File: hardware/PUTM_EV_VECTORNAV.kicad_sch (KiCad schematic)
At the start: 0 parts

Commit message: Fixes after review
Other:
- sheet MCU ports: added VN_GNSS_SYNC; removed VN_SNC_IN, VN_SNC_OUT
- sheet VectorNav ports: added GNSS_SYNC; removed SNC_IN, SNC_OUT
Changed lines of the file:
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@@
-	(wire
-		(pts
-			(xy 82.55 111.76) (xy 120.65 111.76)
-		)
-		(stroke
-			(width 0)
-			(type default)
-		)
-	)
 	(wire
 		(pts
@@
 			)
 		)
-		(pin "CAN_RX" input
+		(pin "CAN_RX" output
 			(at 204.47 87.63 180)
 			(effects
@@
 			)
 		)
-		(pin "CAN_RX" input
-			(at 171.45 85.09 0)
-			(effects
-				(font
-					(size 1.27 1.27)
-				)
-				(justify right)
-			)
-		)
-		(pin "CAN_TX" input
-			(at 171.45 87.63 0)
-			(effects
-				(font
-					(size 1.27 1.27)
-				)
-				(justify right)
-			)
-		)
 		(pin "VN_CS" input
 			(at 120.65 82.55 180)
@@
 			)
 		)
-		(pin "VN_RX" input
-			(at 120.65 97.79 180)
-			(effects
-				(font
-					(size 1.27 1.27)
-				)
-				(justify left)
-			)
-		)
 		(pin "VN_SCK" input
 			(at 120.65 90.17 180)
@@
 			)
 		)
-		(pin "VN_SNC_IN" input
-			(at 120.65 111.76 180)
-			(effects
-				(font
-					(size 1.27 1.27)
-				)
-				(justify left)
-			)
-		)
-		(pin "VN_SNC_OUT" output
-			(at 120.65 114.3 180)
-			(effects
-				(font
-					(size 1.27 1.27)
-				)
-				(justify left)
-			)
-		)
-		(pin "VN_TX" output
-			(at 120.65 95.25 180)
-			(effects
-				(font
-					(size 1.27 1.27)
-				)
-				(justify left)
-			)
-		)
-		(pin "CAN_STBY" input
+		(pin "CAN_STBY" output
 			(at 171.45 90.17 0)
 			(effects
@@
 				)
 				(justify right)
+			)
+		)
+		(pin "VN_RX" input
+			(at 120.65 95.25 180)
+			(effects
+				(font
+					(size 1.27 1.27)
+				)
+				(justify left)
+			)
+		)
+		(pin "VN_TX" output
+			(at 120.65 97.79 180)
+			(effects
+				(font
+					(size 1.27 1.27)
+				)
+				(justify left)
+			)
+		)
+		(pin "CAN_RX" input
+			(at 171.45 87.63 0)
+			(effects
+				(font
+					(size 1.27 1.27)
+				)
+				(justify right)
+			)
+		)
+		(pin "CAN_TX" output
+			(at 171.45 85.09 0)
+			(effects
+				(font
+					(size 1.27 1.27)
+				)
+				(justify right)
+			)
+		)
+		(pin "VN_GNSS_SYNC" input
+			(at 120.65 114.3 180)
+			(effects
+				(font
+					(size 1.27 1.27)
+				)
+				(justify left)
 			)
 		)
@@
 			)
 		)
-		(pin "SNC_IN" input
-			(at 82.55 111.76 0)
-			(effects
-				(font
-					(size 1.27 1.27)
-				)
-				(justify right)
-			)
-		)
-		(pin "SNC_OUT" output
-			(at 82.55 114.3 0)
-			(effects
-				(font
-					(size 1.27 1.27)
-				)
-				(justify right)
-			)
-		)
 		(pin "TX1" output
 			(at 64.77 76.2 90)
@@
 			(effects
 				(font
+					(size 1.27 1.27)
+				)
+				(justify right)
+			)
+		)
+		(pin "GNSS_SYNC" input
+			(at 82.55 114.3 0)
+			(effects
+				(font

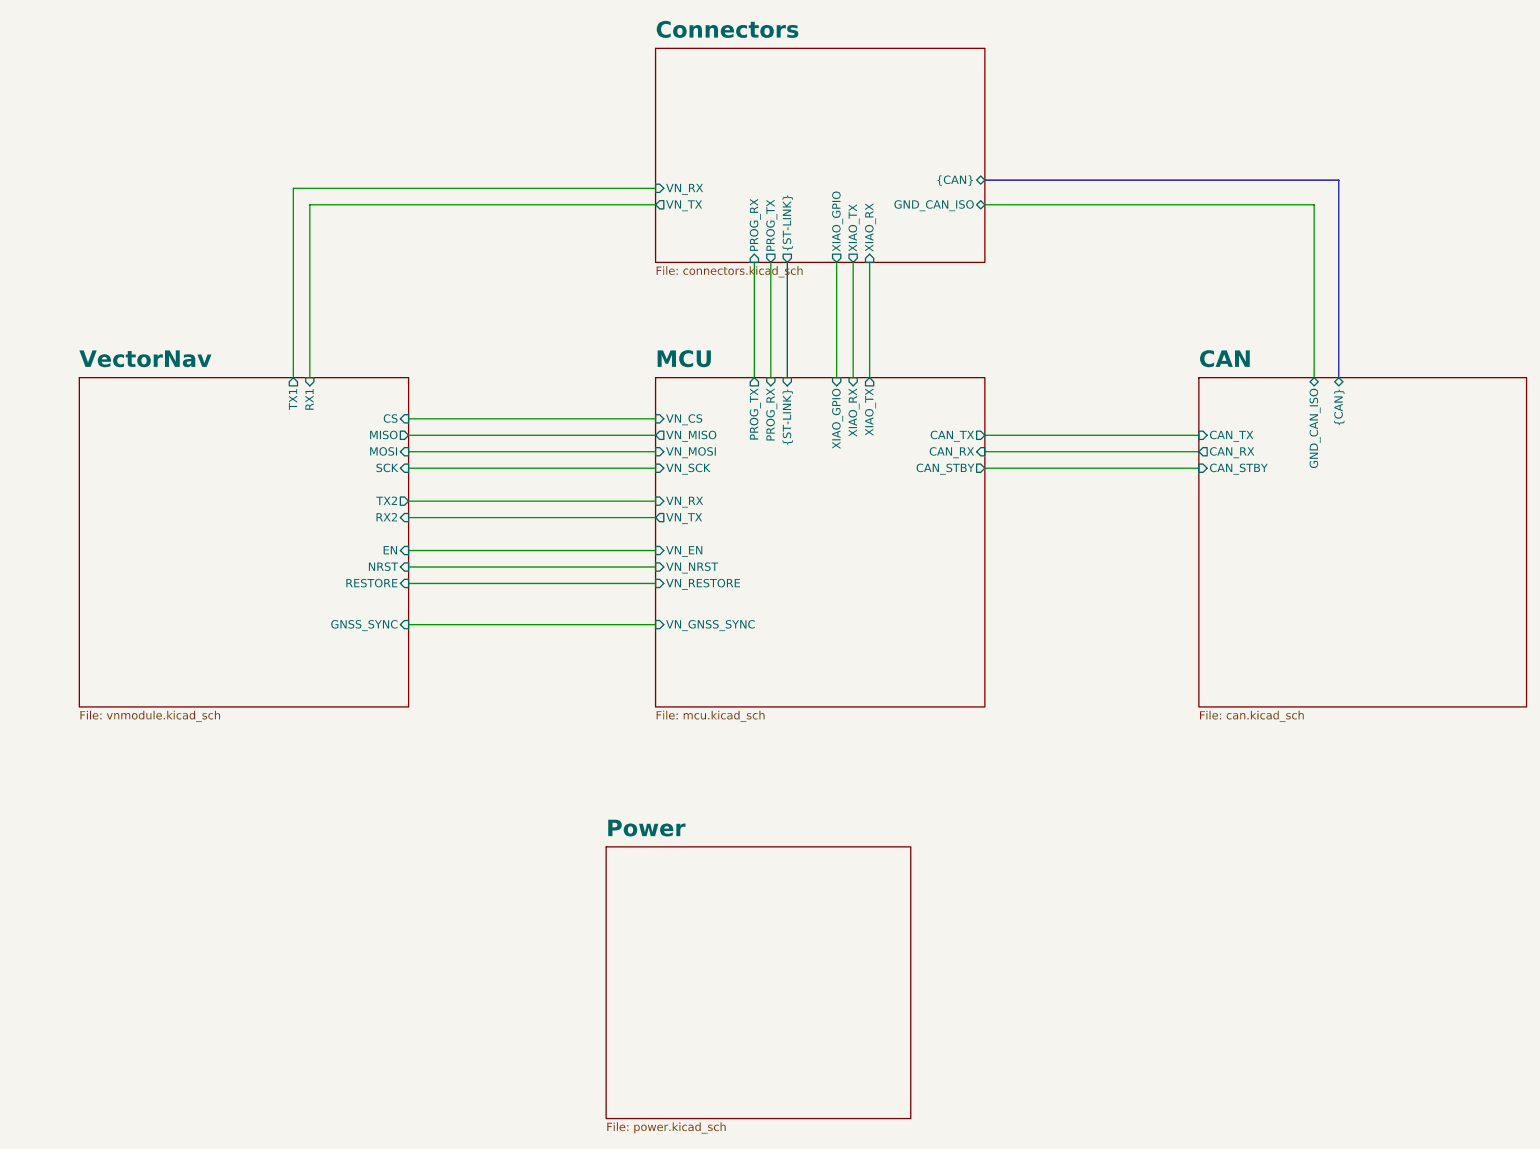
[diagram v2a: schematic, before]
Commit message: Fixes after review and mouser links for most components added
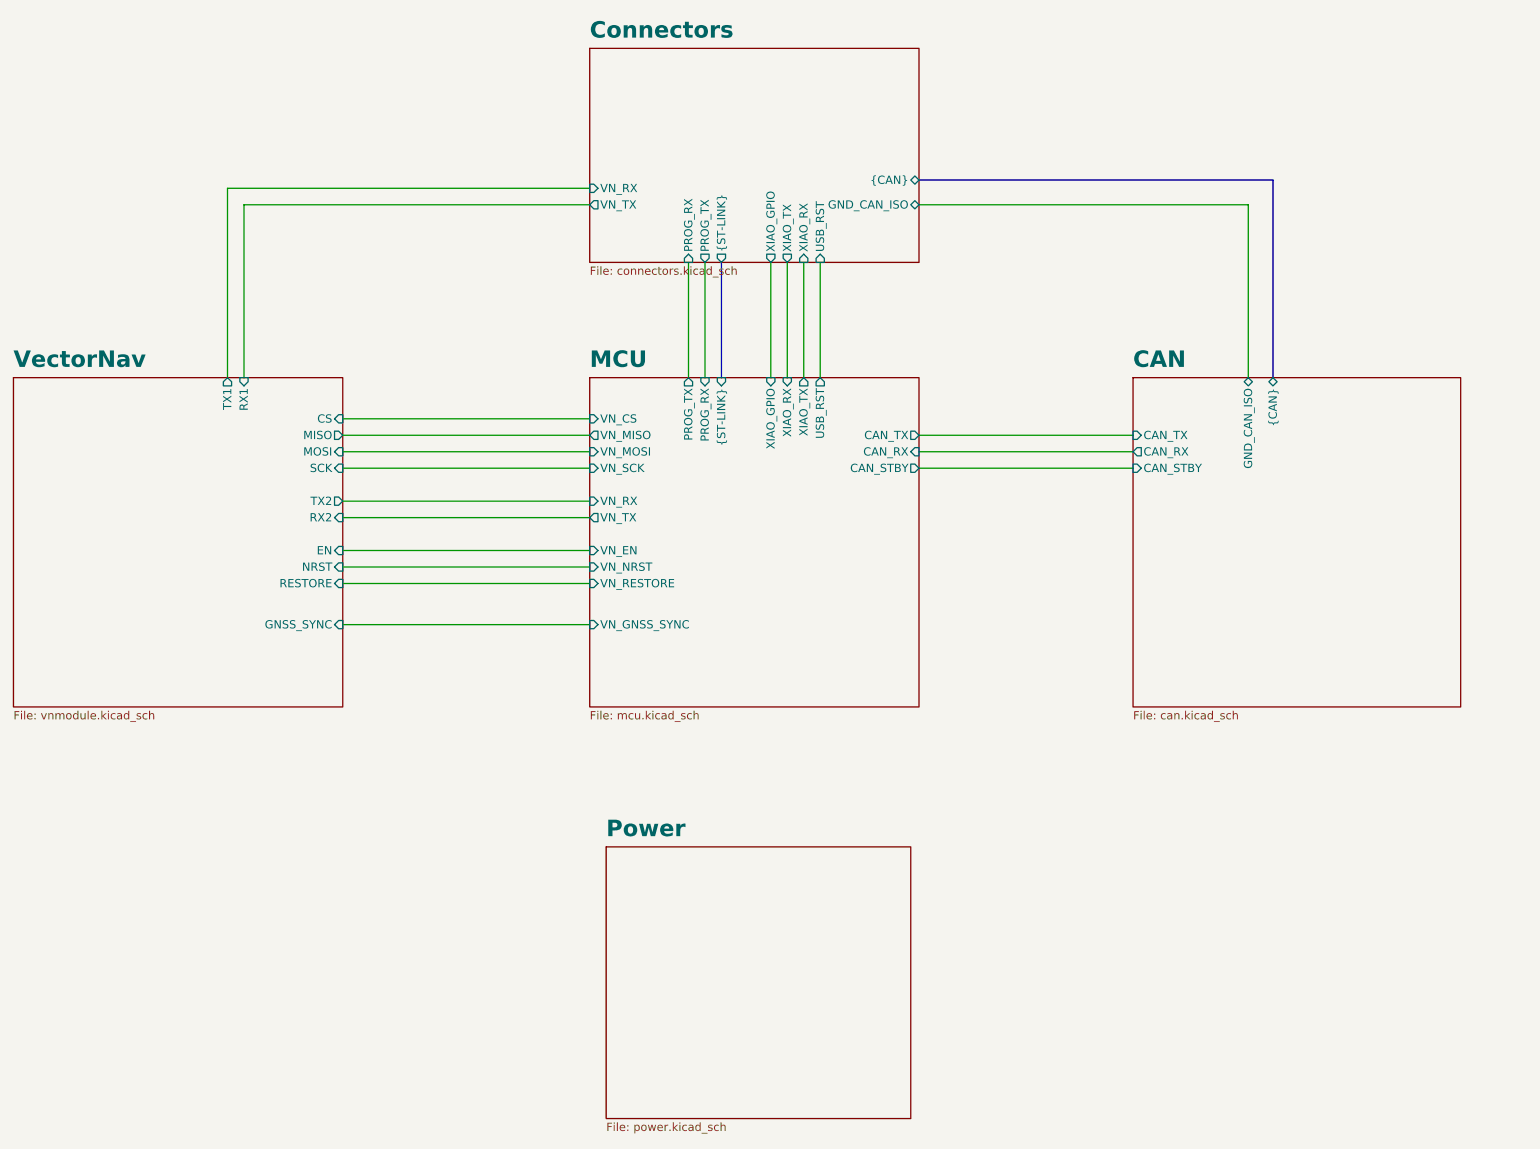
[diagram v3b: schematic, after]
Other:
- sheet Connectors ports: added USB_RST; removed none
- sheet MCU ports: added USB_RST; removed none

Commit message: Some smaller fixes and final aesthetic changes
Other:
- company: Author: -> Author: Kacper Pawlak
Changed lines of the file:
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@@
 	(title_block
 		(rev "${REVISION}")
-		(company "Author:")
-		(comment 1 "Reviewer:")
+		(company "Author: Kacper Pawlak")
+		(comment 1 "Reviewer: Piotr Lesicki")
 	)
 	(wire

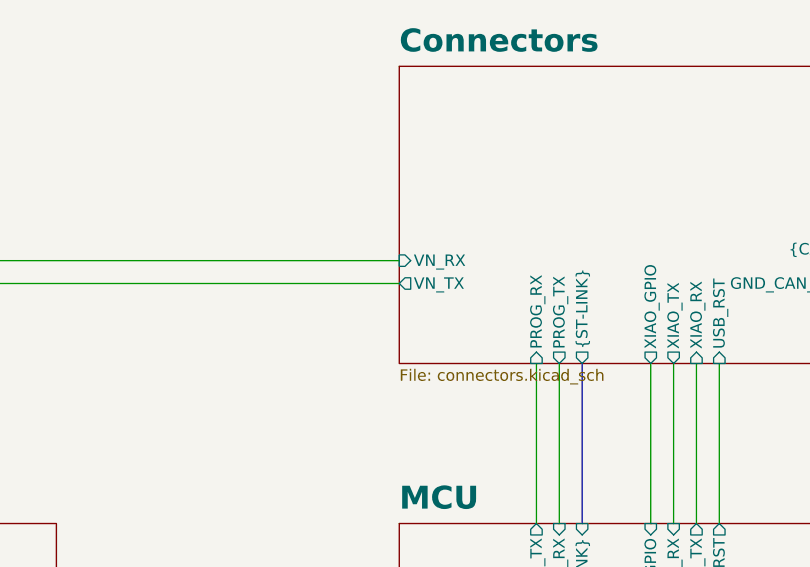
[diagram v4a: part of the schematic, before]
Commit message: little changes with traces and 3D models visibility
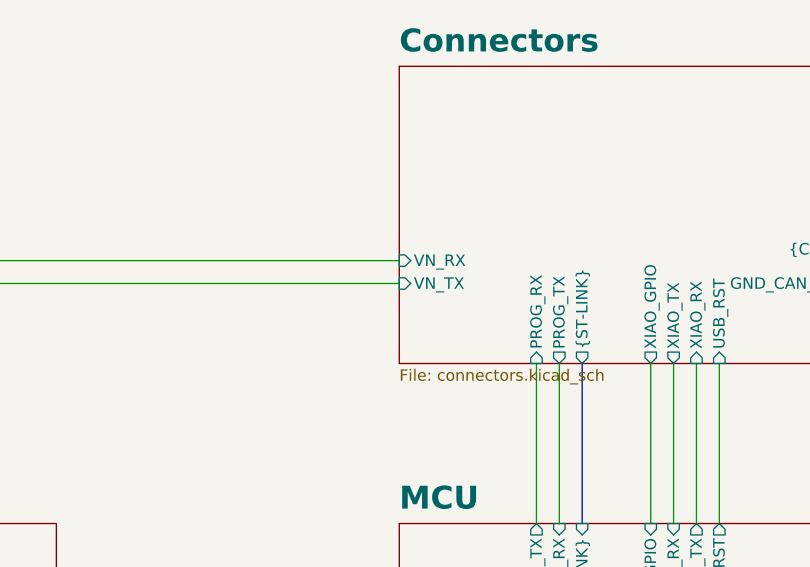
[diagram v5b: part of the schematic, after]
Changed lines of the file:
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@@
 			)
 		)
-		(pin "VN_TX" output
+		(pin "VN_TX" input
 			(at 110.49 49.53 180)
 			(effects
